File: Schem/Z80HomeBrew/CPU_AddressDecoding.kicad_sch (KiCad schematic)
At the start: 18 parts, among them U10 ATF22V10C-10PU, U12 74HC273, U19 SST39SF040-70-4C-PHE, U5 Z084000xP, U6 ATF22V10C-10PU, U7 AS7C4096A-12TCN

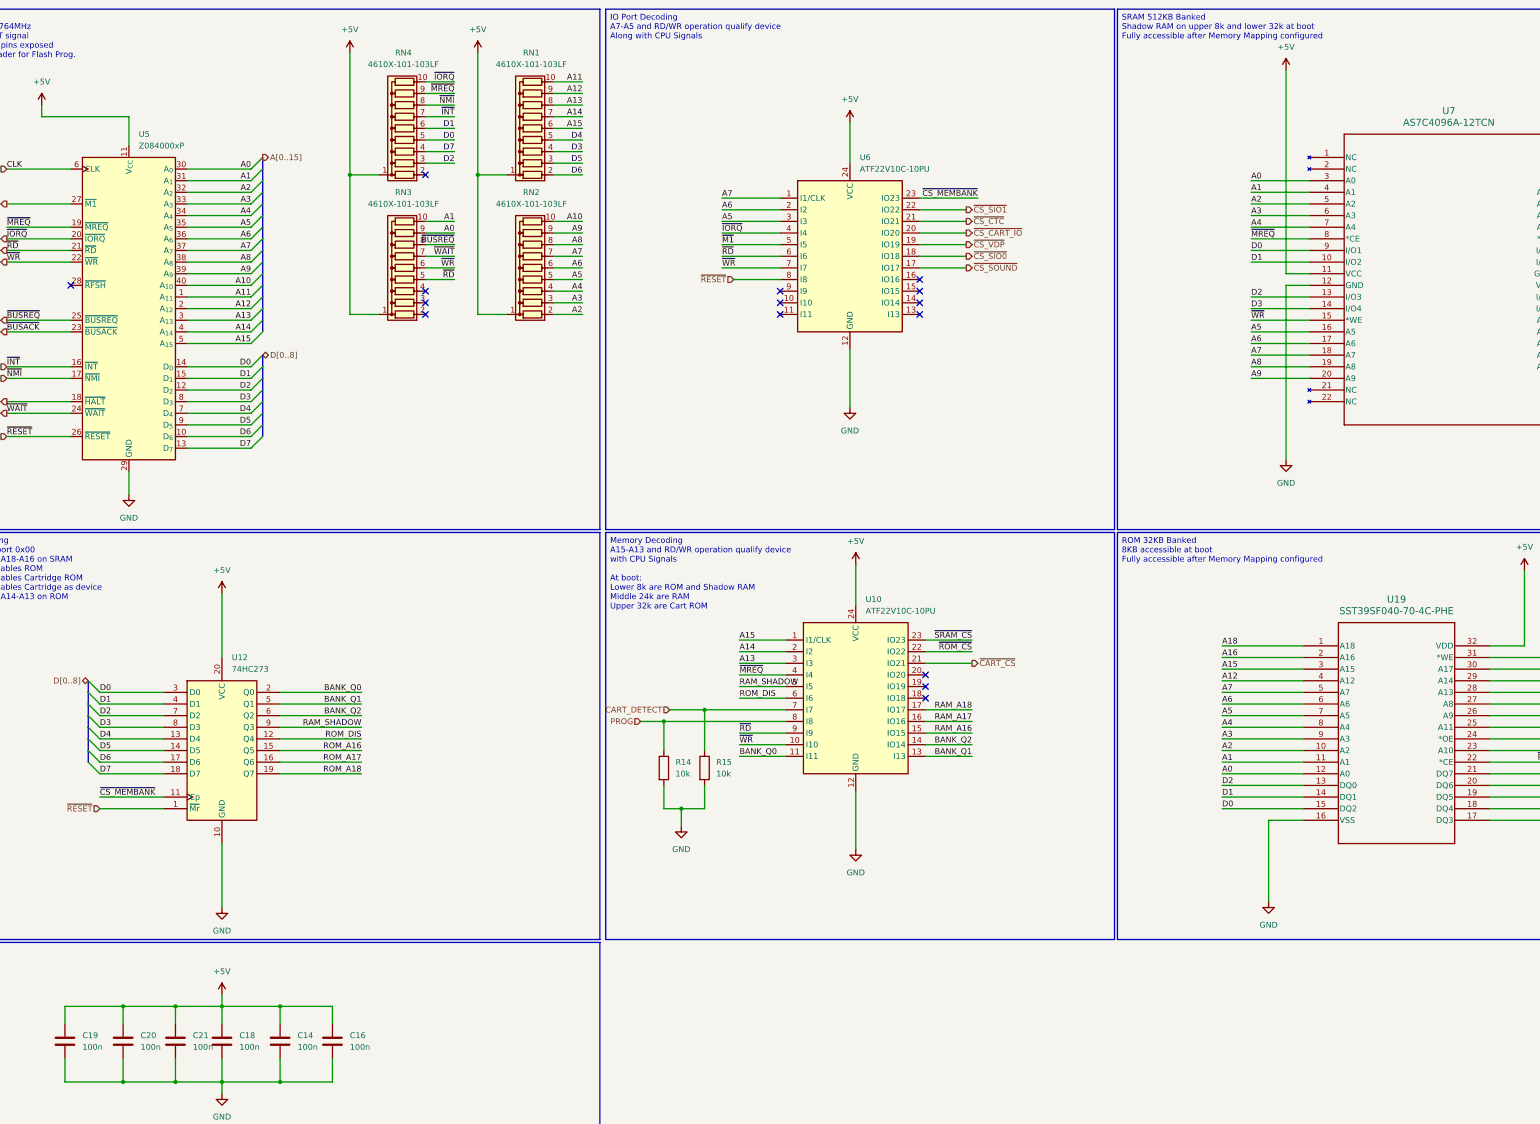
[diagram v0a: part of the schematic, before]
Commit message: Video block added. fixed some issues with parts...
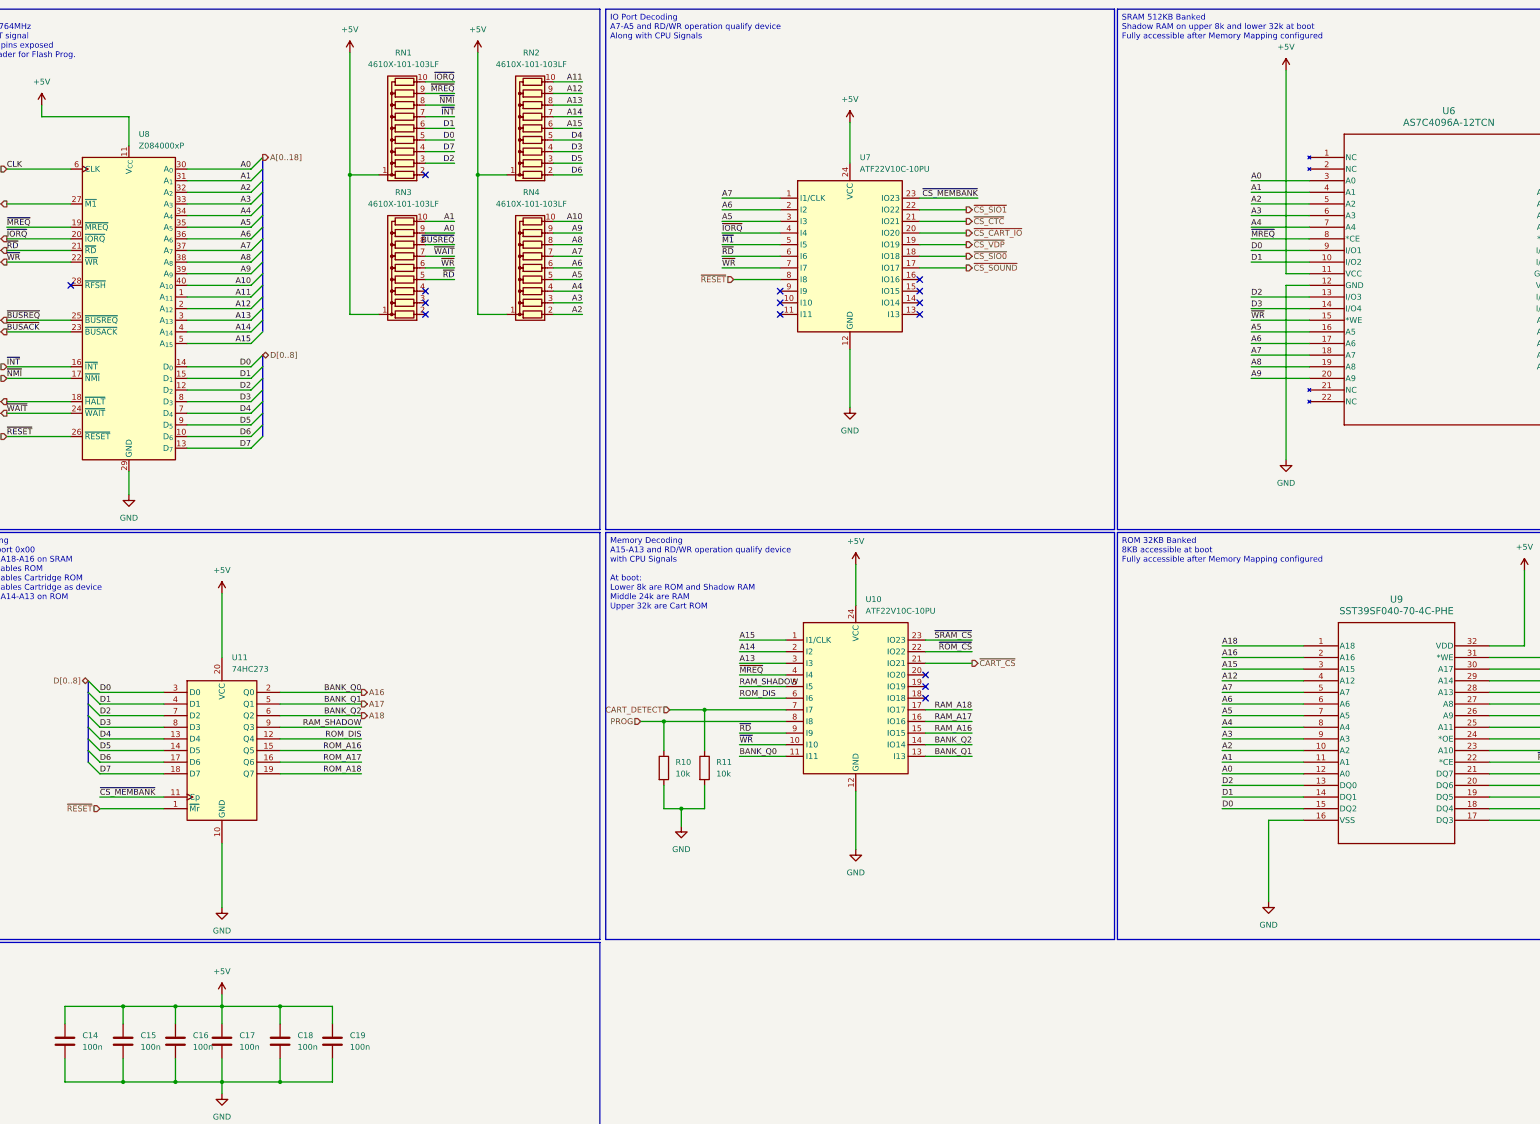
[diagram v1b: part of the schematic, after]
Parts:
- U6: renamed from U7; footprint TSOP-44_MIL400_ALL -> Footprints:TSOP-44_MIL400_ALL
- U8: renamed from U5; footprint Package_DIP:DIP-40_W15.24mm -> Package_DIP:DIP-40_W15.24mm_Socket
- renumbered C19 to C14, C20 to C15, C21 to C16, C18 to C17, C14 to C18, C16 to C19, R14 to R10, R15 to R11, RN4 to RN1, RN1 to RN2, RN2 to RN4, U12 to U11, U6 to U7, U19 to U9
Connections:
- net BANK_Q0 is gone; now on net A16: U10.11 (I11), U11.2 (Q0)
- net BANK_Q1 is gone; now on net A17: U10.13 (I13), U11.5 (Q1)
- net BANK_Q2 is gone; now on net A18: U10.14 (IO14), U11.6 (Q2)
